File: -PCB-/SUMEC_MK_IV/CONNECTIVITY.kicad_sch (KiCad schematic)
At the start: 7 parts, among them J12 TYPE-C-31-M-12, U6 USBLC6-2SC6

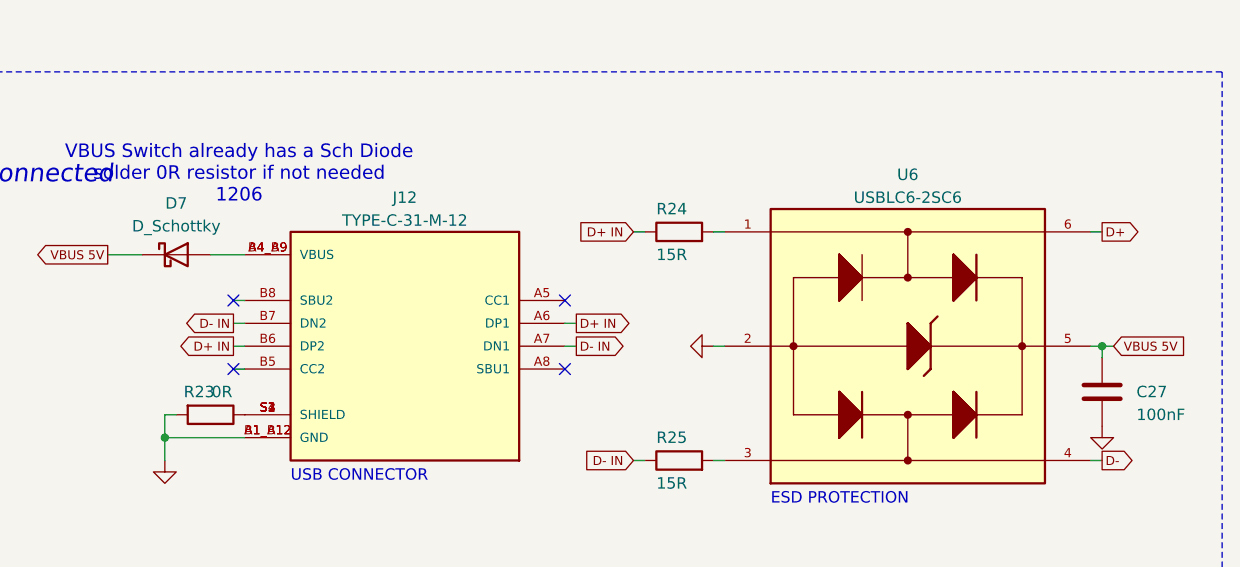
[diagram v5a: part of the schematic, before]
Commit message: Footprints added
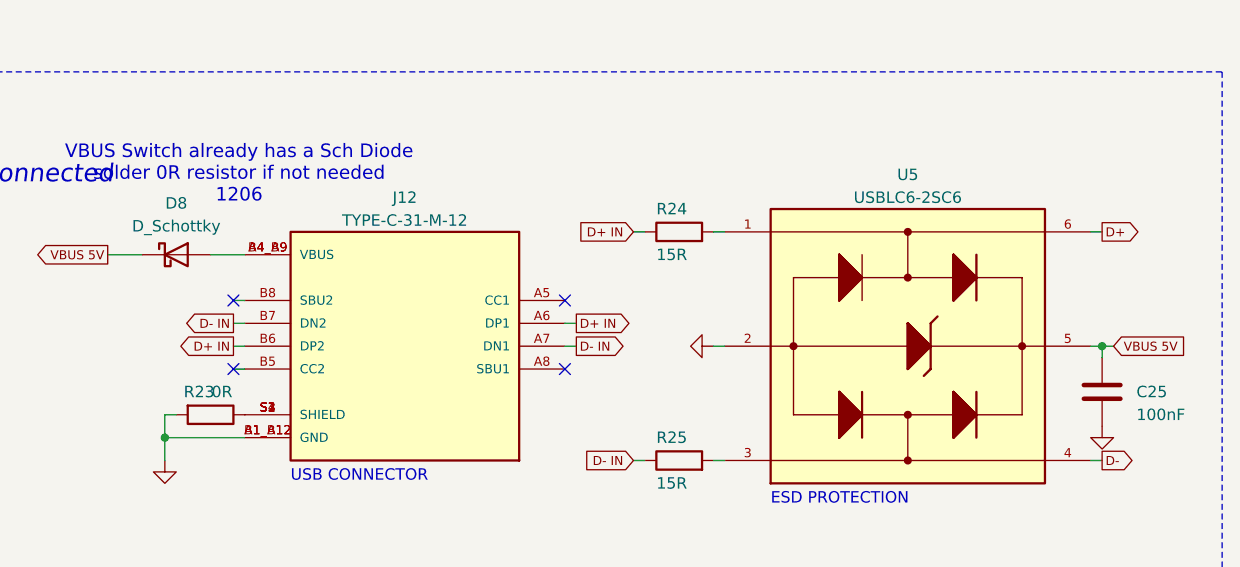
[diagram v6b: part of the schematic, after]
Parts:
- D8: renamed from D7; footprint (none) -> Diode_SMD:D_1206_3216Metric_Pad1.42x1.75mm_HandSolder
- R23: footprint Resistor_SMD:R_1206_3216Metric_Pad1.30x1.75mm_HandSolder -> Resistor_SMD:R_0805_2012Metric_Pad1.20x1.40mm_HandSolder
- renumbered C27 to C25, U6 to U5
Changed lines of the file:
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@@
 		(dnp no)
 		(fields_autoplaced yes)
-		(property "Reference" "U6"
+		(property "Reference" "U5"
 			(at 200.66 80.01 0)
 			(effects
@@
 			(project "SUMEC_MK_IV"
 				(path "/900bd7ac-cdf9-4a2f-8b1f-2c21e3760046/ce2ae977-07a3-41c1-b3e1-68b5a1d5517b"
-					(reference "U6")
+					(reference "U5")
 					(unit 1)
 				)
@@
 		(on_board yes)
 		(dnp no)
-		(property "Reference" "D7"
+		(property "Reference" "D8"
 			(at 119.38 83.185 0)
 			(effects
@@
 			)
 		)
-		(property "Footprint" ""
+		(property "Footprint" "Diode_SMD:D_1206_3216Metric_Pad1.42x1.75mm_HandSolder"
 			(at 119.38 88.9 0)
 			(effects
@@
 			(project "SUMEC_MK_IV"
 				(path "/900bd7ac-cdf9-4a2f-8b1f-2c21e3760046/ce2ae977-07a3-41c1-b3e1-68b5a1d5517b"
-					(reference "D7")
+					(reference "D8")
 					(unit 1)
 				)
@@
 		(dnp no)
 		(fields_autoplaced yes)
-		(property "Reference" "#PWR072"
+		(property "Reference" "#PWR074"
 			(at 222.25 114.3 0)
 			(effects
@@
 			(project "SUMEC_MK_IV"
 				(path "/900bd7ac-cdf9-4a2f-8b1f-2c21e3760046/ce2ae977-07a3-41c1-b3e1-68b5a1d5517b"
-					(reference "#PWR072")
+					(reference "#PWR074")
 					(unit 1)
 				)
@@
 		(on_board yes)
 		(dnp no)
-		(property "Reference" "C27"
+		(property "Reference" "C25"
 			(at 226.06 104.14 0)
 			(effects
@@
 			(project "SUMEC_MK_IV"
 				(path "/900bd7ac-cdf9-4a2f-8b1f-2c21e3760046/ce2ae977-07a3-41c1-b3e1-68b5a1d5517b"
-					(reference "C27")
+					(reference "C25")
 					(unit 1)
 				)
@@
 			)
 		)
-		(property "Footprint" "Resistor_SMD:R_1206_3216Metric_Pad1.30x1.75mm_HandSolder"
+		(property "Footprint" "Resistor_SMD:R_0805_2012Metric_Pad1.20x1.40mm_HandSolder"
 			(at 123.19 104.902 90)
 			(effects
@@
 		(dnp no)
 		(fields_autoplaced yes)
-		(property "Reference" "#PWR071"
+		(property "Reference" "#PWR073"
 			(at 172.72 99.06 0)
 			(effects
@@
 			(project "SUMEC_MK_IV"
 				(path "/900bd7ac-cdf9-4a2f-8b1f-2c21e3760046/ce2ae977-07a3-41c1-b3e1-68b5a1d5517b"
-					(reference "#PWR071")
+					(reference "#PWR073")
 					(unit 1)
 				)
@@
 		(dnp no)
 		(fields_autoplaced yes)
-		(property "Reference" "#PWR070"
+		(property "Reference" "#PWR072"
 			(at 118.11 118.11 0)
 			(effects
@@
 			(project "SUMEC_MK_IV"
 				(path "/900bd7ac-cdf9-4a2f-8b1f-2c21e3760046/ce2ae977-07a3-41c1-b3e1-68b5a1d5517b"
-					(reference "#PWR070")
+					(reference "#PWR072")
 					(unit 1)
 				)

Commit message: v3.0.9 SUMEC PCB
Ufff, so, basically a full rewrite of the PCB, check it our its pretty sick, I think
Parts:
- removed R23: 0R, Resistor_SMD:R_0805_2012Metric_Pad1.20x1.40mm_HandSolder, symbol Device:R
- added J12: Conn_01x02_Pin, TestPoint:TestPoint_2Pads_Pitch2.54mm_Drill0.8mm, symbol Connector:Conn_01x02_Pin
- renumbered C25 to C23, D8 to D7, J12 to J13, R24 to R17, R25 to R18, U5 to U4
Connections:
- new net RX: J12.2 (Pin_2)
- new net TX: J12.1 (Pin_1)
- no-connect marks 4 -> 5
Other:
- note added: "UART"
- moved on the sheet: C23, D7, J13, R17, R18, U4

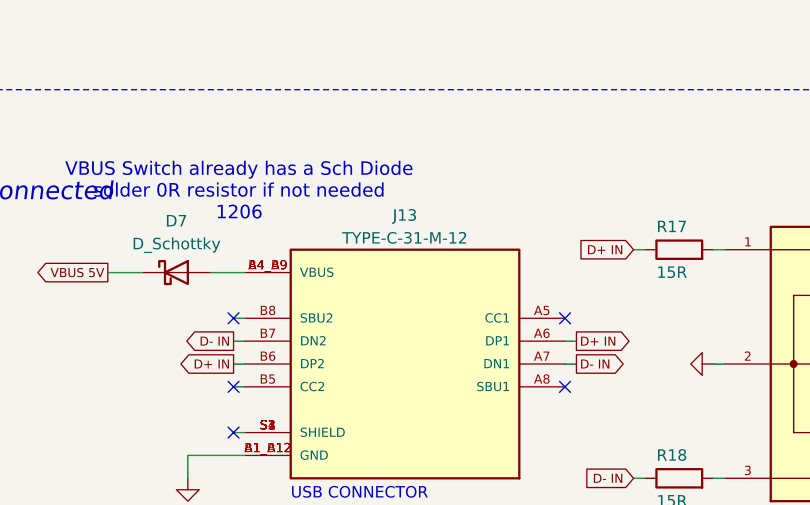
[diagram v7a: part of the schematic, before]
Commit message: Dimensions back and front, 3d models for footprints.
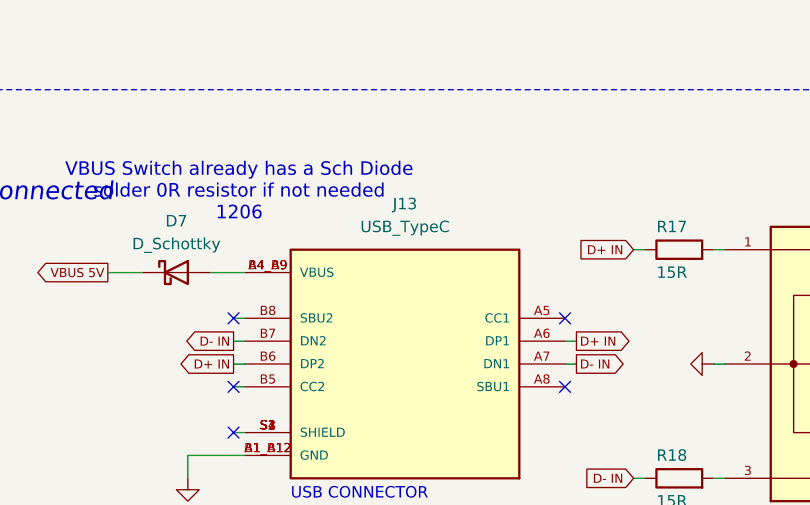
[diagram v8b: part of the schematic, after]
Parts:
- removed J13: TYPE-C-31-M-12, sumec-smdV2_library:USB_Type_C, symbol sumec_library:TYPE-C-31-M-12
- added J13: USB_TypeC, sumec_brd:USB_Type_C, symbol sumec_sch_lib:USB_TypeC
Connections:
- net D+ IN: now also J13.A6 (DP1), J13.B6 (DP2)
- net D- IN: now also J13.A7 (DN1), J13.B7 (DN2)
- net GND: now also J13.A1_B12 (GND), J13.B1_A12 (GND)
- net at D7.2 (A): now also J13.A4_B9 (VBUS), J13.B4_A9 (VBUS)
- new net: J13.S1 (SHIELD), J13.S2 (SHIELD), J13.S3 (SHIELD), J13.S4 (SHIELD)
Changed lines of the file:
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@@
-	)
-	(symbol
-		(lib_id "sumec_library:TYPE-C-31-M-12")
-		(at 139.7 72.39 0)
-		(mirror y)
-		(unit 1)
-		(exclude_from_sim no)
-		(in_bom yes)
-		(on_board yes)
-		(dnp no)
-		(property "Reference" "J13"
-			(at 139.7 55.88 0)
-			(effects
-				(font
-					(face "Bahnschrift")
-					(size 1.27 1.27)
-				)
-			)
-		)
-		(property "Value" "TYPE-C-31-M-12"
-			(at 139.7 58.42 0)
-			(effects
-				(font
-					(face "Bahnschrift")
-					(size 1.27 1.27)
-				)
-			)
-		)
-		(property "Footprint" "sumec-smdV2_library:USB_Type_C"
-			(at 139.7 72.39 0)
-			(effects
-				(font
-					(face "Bahnschrift")
-					(size 1.27 1.27)
-				)
-				(justify bottom)
-				(hide yes)
-			)
-		)
-		(property "Datasheet" ""
-			(at 139.7 72.39 0)
-			(effects
-				(font
-					(face "Bahnschrift")
-					(size 1.27 1.27)
-				)
-				(hide yes)
-			)
-		)
-		(property "Description" "\nUSB Connectors 24 Receptacle 1 8.94*7.3mm RoHS\n"
-			(at 139.7 72.39 0)
-			(effects
-				(font
-					(face "Bahnschrift")
-					(size 1.27 1.27)
-				)
-				(justify bottom)
-				(hide yes)
-			)
-		)
-		(property "MF" "HRO Electronics Co., Ltd."
-			(at 139.7 72.39 0)
-			(effects
-				(font
-					(face "Bahnschrift")
-					(size 1.27 1.27)
-				)
-				(justify bottom)
-				(hide yes)
-			)
-		)
-		(property "MAXIMUM_PACKAGE_HEIGHT" "3.26 mm"
-			(at 139.7 72.39 0)
-			(effects
-				(font
-					(face "Bahnschrift")
-					(size 1.27 1.27)
-				)
-				(justify bottom)
-				(hide yes)
-			)
-		)
-		(property "Package" "Package"
-			(at 139.7 72.39 0)
-			(effects
-				(font
-					(face "Bahnschrift")
-					(size 1.27 1.27)
-				)
-				(justify bottom)
-				(hide yes)
-			)
-		)
-		(property "Price" "None"
-			(at 139.7 72.39 0)
-			(effects
-				(font
-					(face "Bahnschrift")
-					(size 1.27 1.27)
-				)
-				(justify bottom)
-				(hide yes)
-			)
-		)
-		(property "Check_prices" "https://www.snapeda.com/parts/TYPE-C-31-M-12/HRO+Electronics+Co.%252C+Ltd./view-part/?ref=eda"
-			(at 139.7 72.39 0)
-			(effects
-				(font
-					(face "Bahnschrift")
-					(size 1.27 1.27)
-				)
-				(justify bottom)
-				(hide yes)
-			)
-		)
-		(property "STANDARD" "Manufacturer Recommendations"
-			(at 139.7 72.39 0)
-			(effects
-				(font
-					(face "Bahnschrift")
-					(size 1.27 1.27)
-				)
-				(justify bottom)
-				(hide yes)
-			)
-		)
-		(property "PARTREV" "2020.12.08"
-			(at 139.7 72.39 0)
-			(effects
-				(font
-					(face "Bahnschrift")
-					(size 1.27 1.27)
-				)
-				(justify bottom)
-				(hide yes)
-			)
-		)
-		(property "SnapEDA_Link" "https://www.snapeda.com/parts/TYPE-C-31-M-12/HRO+Electronics+Co.%252C+Ltd./view-part/?ref=snap"
-			(at 139.7 72.39 0)
-			(effects
-				(font
-					(face "Bahnschrift")
-					(size 1.27 1.27)
-				)
-				(justify bottom)
-				(hide yes)
-			)
-		)
-		(property "MP" "TYPE-C-31-M-12"
-			(at 139.7 72.39 0)
-			(effects
-				(font
-					(face "Bahnschrift")
-					(size 1.27 1.27)
-				)
-				(justify bottom)
-				(hide yes)
-			)
-		)
-		(property "SNAPEDA_PN" "TYPE-C-31-M-12"
-			(at 139.7 72.39 0)
-			(effects
-				(font
-					(face "Bahnschrift")
-					(size 1.27 1.27)
-				)
-				(justify bottom)
-				(hide yes)
-			)
-		)
-		(property "Availability" "Not in stock"
-			(at 139.7 72.39 0)
-			(effects
-				(font
-					(face "Bahnschrift")
-					(size 1.27 1.27)
-				)
-				(justify bottom)
-				(hide yes)
-			)
-		)
-		(property "MANUFACTURER" "HRO Electronics Co., Ltd."
-			(at 139.7 72.39 0)
-			(effects
-				(font
-					(face "Bahnschrift")
-					(size 1.27 1.27)
-				)
-				(justify bottom)
-				(hide yes)
-			)
-		)
-		(pin "A1_B12"
-		)
-		(pin "A4_B9"
-		)
-		(pin "A5"
-		)
-		(pin "A6"
-		)
-		(pin "A7"
-		)
-		(pin "A8"
-		)
-		(pin "B1_A12"
-		)
-		(pin "B4_A9"
-		)
-		(pin "B5"
-		)
-		(pin "B6"
-		)
-		(pin "B7"
-		)
-		(pin "B8"
-		)
-		(pin "S1"
-		)
-		(pin "S2"
-		)
-		(pin "S3"
-		)
-		(pin "S4"
-		)
-		(instances
-			(project "SUMEC_MK_IV"
-				(path "/900bd7ac-cdf9-4a2f-8b1f-2c21e3760046/ce2ae977-07a3-41c1-b3e1-68b5a1d5517b"
-					(reference "J13")
-					(unit 1)
-				)
-			)
-		)
 	)
 	(symbol
@@
 					(unit 1)
 				)
+			)
+		)
+	)
+	(symbol
+		(lib_id "sumec_sch_lib:USB_TypeC")
+		(at 139.7 72.39 0)
+		(mirror y)
+		(unit 1)
+		(exclude_from_sim no)
+		(in_bom yes)
+		(on_board yes)
+		(dnp no)
+		(fields_autoplaced yes)
+		(property "Reference" "J13"
+			(at 139.7 54.61 0)
+			(effects
+				(font
+					(size 1.27 1.27)
+				)
+			)
+		)
+		(property "Value" "USB_TypeC"
+			(at 139.7 57.15 0)
+			(effects
+				(font
+					(size 1.27 1.27)
+				)
+			)
+		)
+		(property "Footprint" "sumec_brd:USB_Type_C"
+			(at 139.7 72.39 0)
+			(effects
+				(font
+					(size 1.27 1.27)
+				)
+				(justify bottom)
+				(hide yes)
+			)
+		)
+		(property "Datasheet" "TYPE-C-31-M-12"
+			(at 139.7 72.39 0)
+			(effects
+				(font
+					(size 1.27 1.27)
+				)
+				(hide yes)
+			)
+		)
+		(property "Description" "USB Connectors 24 Receptacle 1 8.94*7.3mm RoHS"
+			(at 139.7 72.39 0)
+			(effects
+				(font
+					(size 1.27 1.27)
+				)
+				(justify bottom)
+				(hide yes)
+			)
+		)
+		(property "MF" "HRO Electronics Co., Ltd."
+			(at 139.7 72.39 0)
+			(effects
+				(font
+					(size 1.27 1.27)
+				)
+				(justify bottom)
+				(hide yes)
+			)
+		)
+		(property "MAXIMUM_PACKAGE_HEIGHT" "3.26 mm"
+			(at 139.7 72.39 0)
+			(effects
+				(font
+					(size 1.27 1.27)
+				)
+				(justify bottom)
+				(hide yes)
+			)
+		)
+		(property "Package" "Package"
+			(at 139.7 72.39 0)
+			(effects
+				(font
+					(size 1.27 1.27)
+				)
+				(justify bottom)
+				(hide yes)
+			)
+		)
+		(property "Price" "None"
+			(at 139.7 72.39 0)
+			(effects
+				(font
+					(size 1.27 1.27)
+				)
+				(justify bottom)
+				(hide yes)
+			)
+		)
+		(property "Check_prices" "https://www.snapeda.com/parts/TYPE-C-31-M-12/HRO+Electronics+Co.%252C+Ltd./view-part/?ref=eda"
+			(at 137.16 72.39 0)
+			(effects
+				(font
+					(size 1.27 1.27)
+				)
+				(justify bottom)
+				(hide yes)
+			)
+		)
+		(property "STANDARD" "Manufacturer Recommendations"
+			(at 139.7 72.39 0)
+			(effects
+				(font
+					(size 1.27 1.27)
+				)
+				(justify bottom)
+				(hide yes)
+			)
+		)
+		(property "PARTREV" "2020.12.08"
+			(at 139.7 72.39 0)
+			(effects
+				(font
+					(size 1.27 1.27)
+				)
+				(justify bottom)
+				(hide yes)
+			)
+		)
+		(property "SnapEDA_Link" "https://www.snapeda.com/parts/TYPE-C-31-M-12/HRO+Electronics+Co.%252C+Ltd./view-part/?ref=snap"
+			(at 139.7 72.39 0)
+			(effects
+				(font
+					(size 1.27 1.27)
+				)
+				(justify bottom)
+				(hide yes)
+			)
+		)
+		(property "MP" "TYPE-C-31-M-12"
+			(at 139.7 72.39 0)
+			(effects
+				(font
+					(size 1.27 1.27)
+				)
+				(justify bottom)
+				(hide yes)
+			)
+		)
+		(property "SNAPEDA_PN" "TYPE-C-31-M-12"
+			(at 139.7 72.39 0)
+			(effects
+				(font
+					(size 1.27 1.27)
+				)
+				(justify bottom)
+				(hide yes)
+			)
+		)
+		(property "Availability" "Not in stock"
+			(at 139.7 72.39 0)
+			(effects
+				(font
+					(size 1.27 1.27)
+				)
+				(justify bottom)
+				(hide yes)
+			)
+		)
+		(property "MANUFACTURER" "HRO Electronics Co., Ltd."
+			(at 139.7 72.39 0)
+			(effects
+				(font
+					(size 1.27 1.27)
+				)
+				(justify bottom)
+				(hide yes)
+			)
+		)
+		(pin "B5"
+		)
+		(pin "S1"
+		)
+		(pin "S3"
+		)
+		(pin "A4_B9"
+		)
+		(pin "B1_A12"
+		)
+		(pin "S2"
+		)
+		(pin "B4_A9"
+		)
+		(pin "A5"
+		)
+		(pin "B6"
+		)
+		(pin "S4"
+		)
+		(pin "A7"
+		)
+		(pin "A1_B12"
+		)
+		(pin "A6"
+		)
+		(pin "B8"
+		)
+		(pin "A8"
+		)
+		(pin "B7"
+		)
+		(instances
+			(project ""
+				(path "/900bd7ac-cdf9-4a2f-8b1f-2c21e3760046/ce2ae977-07a3-41c1-b3e1-68b5a1d5517b"
+					(reference "J13")
+					(unit 1)
+				)
